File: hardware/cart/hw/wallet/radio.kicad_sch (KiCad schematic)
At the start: 81 parts, among them Q101 SIA975DJ-T1-GE3, Q102 2N7002, U101 TPS2116DRLR, U102 TPS2553DBVR, U103 TPS63802DLAR, U104 ESP32-C3-MINI-1U-N4, U105 SN74LVC1G125DBVR, U106 SN74LVC3G34DCTR, U107 CH334P, U108 TLV3012BIDBVR, U109 TLV431BIDBZR, U110 SE050E2HQ1/Z01Z3Z, U111 LIS3DHTR, Y101 12MHz 10pF 10ppm

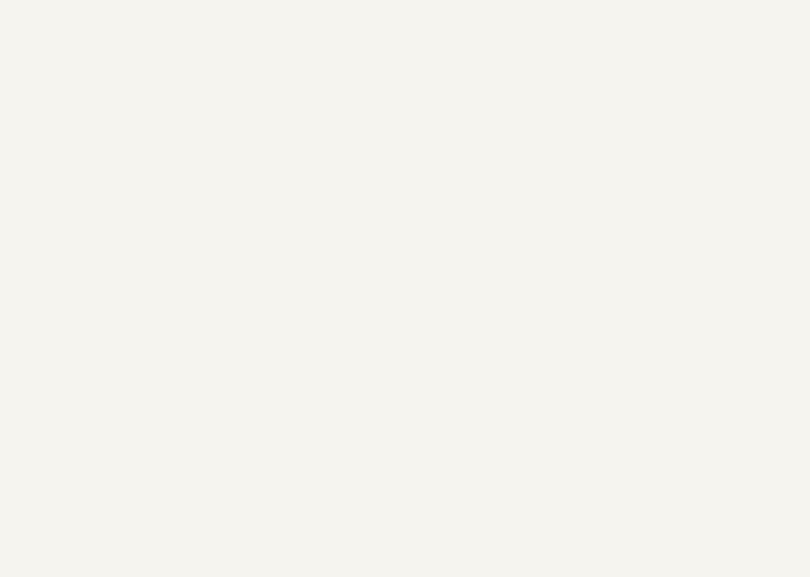
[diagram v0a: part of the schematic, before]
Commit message: Board: fixes from an independent datasheet review (2026-10-16)
A fresh reviewer, without our notes or gates, checked the schematic and board
against every datasheet. Fixed:
- radio-area ground: F.Cu pour, 60 stitching vias, 9 vias in the ESP32-C3
  centre pad, vias at the TPS63802 GND pins (219 -> 296 GND vias)
- VREG_LX cut-out on In1-In4 (RP2350 DS 6.3.8, Fig. 27); ESP CS and LED_DIN
  re-routed around it
- R110 91k: C4147 (below JLC minimum buy) -> C453777
- R138 4.7k pull-down on the TXB0108 OE (SCES643 sec 9)
- Y1: ABM8-272-T3 (C20625731), the crystal Raspberry Pi specifies
- USB upstream pair: both lines on In2 over solid ground, 2 vias each

Kept, with reasons in the LOGBOOK: radio input threshold, D1 on 3V3, antenna.
All gates, power audits (81/114) and fab outputs re-run. New tools:
add_pour, gnd_stitch, lx_keepout, inner_link.

Co-Authored-By: Claude Opus 5.5 (1M context) <noreply@anthropic.com>
Claude-Session: https://claude.ai/code/session_01K3DS9Lp5DvbMPN1T6z91y9
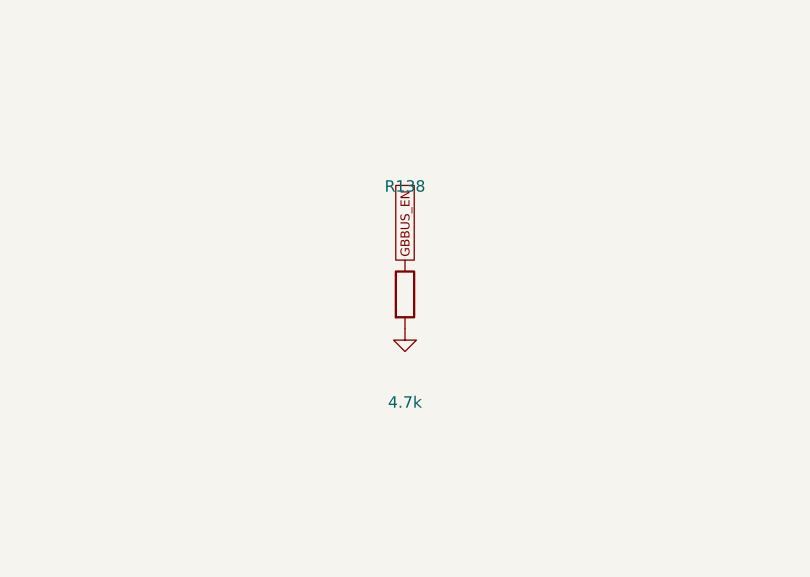
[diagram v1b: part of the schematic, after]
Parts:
- added R138: 4.7k, Resistor_SMD:R_0402_1005Metric, symbol Device:R
- R110: LCSC C4147 -> C453777
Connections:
- net GND: now also R138.2
- new net GBBUS_EN: R138.1
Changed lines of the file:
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@@
 			)
 		)
-		(property "LCSC" "C4147"
+		(property "LCSC" "C453777"
 			(at 88.9 172.72 0)
 			(effects
@@
 					(unit 1)
 				)
+			)
+		)
+	)
+	(global_label "GBBUS_EN"
+		(shape passive)
+		(at 88.9 544.83 90)
+		(fields_autoplaced yes)
+		(effects
+			(font
+				(size 1.0 1.0)
+			)
+			(justify left)
+		)
+		(property "Intersheetrefs" "${INTERSHEET_REFS}"
+			(at 88.9 544.83 0)
+			(effects
+				(font
+					(size 1.0 1.0)
+				)
+				(hide yes)
+			)
+		)
+	)
+	(symbol
+		(lib_id "power:GND")
+		(at 88.9 552.45 0)
+		(unit 1)
+		(exclude_from_sim no)
+		(in_bom yes)
+		(on_board yes)
+		(dnp no)
+		(property "Reference" "#PWR01106"
+			(at 88.9 557.45 0)
+			(effects
+				(font
+					(size 1.27 1.27)
+				)
+				(hide yes)
+			)
+		)
+		(property "Value" "GND"
+			(at 88.9 555.45 0)
+			(effects
+				(font
+					(size 1.27 1.27)
+				)
+				(hide yes)
+			)
+		)
+		(property "Footprint" ""
+			(at 88.9 552.45 0)
+			(effects
+				(font
+					(size 1.27 1.27)
+				)
+				(hide yes)
+			)
+		)
+		(property "Datasheet" ""
+			(at 88.9 552.45 0)
+			(effects
+				(font
+					(size 1.27 1.27)
+				)
+				(hide yes)
+			)
+		)
+		(property "Description" ""
+			(at 88.9 552.45 0)
+			(effects
+				(font
+					(size 1.27 1.27)
+				)
+				(hide yes)
+			)
+		)
+		(pin "1"
+		)
+		(instances
+			(project "GameboyCartridgeV2.1"
+				(path "/ec16e1da-c950-4911-941a-a1ab0200cc01/5f3a9c2e-7b1d-4e6a-9c0f-1a2b3c4d5e60"
+					(reference "#PWR01106")
+					(unit 1)
+				)
+			)
+		)
+	)
+	(symbol
+		(lib_id "Device:R")
+		(at 88.9 548.64 0)
+		(unit 1)
+		(exclude_from_sim no)
+		(in_bom yes)
+		(on_board yes)
+		(dnp no)
+		(property "Reference" "R138"
+			(at 88.9 536.64 0)
+			(effects
+				(font
+					(size 1.27 1.27)
+				)
+			)
+		)
+		(property "Value" "4.7k"
+			(at 88.9 560.64 0)
+			(effects
+				(font
+					(size 1.27 1.27)
+				)
+			)
+		)
+		(property "Footprint" "Resistor_SMD:R_0402_1005Metric"
+			(at 88.9 548.64 0)
+			(effects
+				(font
+					(size 1.27 1.27)
+				)
+				(hide yes)
+			)
+		)
+		(property "Datasheet" ""
+			(at 88.9 548.64 0)
+			(effects
+				(font
+					(size 1.27 1.27)
+				)
+				(hide yes)
+			)
+		)
+		(property "Description" ""
+			(at 88.9 548.64 0)
+			(effects
+				(font
+					(size 1.27 1.27)
+				)
+				(hide yes)
+			)
+		)
+		(property "LCSC" "C25900"
+			(at 88.9 548.64 0)
+			(effects
+				(font
+					(size 1.27 1.27)
+				)
+				(hide yes)
+			)
+		)
+		(pin "1"
+		)
+		(pin "2"
+		)
+		(instances
+			(project "GameboyCartridgeV2.1"
+				(path "/ec16e1da-c950-4911-941a-a1ab0200cc01/5f3a9c2e-7b1d-4e6a-9c0f-1a2b3c4d5e60"
+					(reference "R138")
+					(unit 1)
+				)
